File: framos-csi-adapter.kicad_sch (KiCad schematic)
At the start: 68 parts, among them J1 DF40HC(4.0)-60DS-0.4V(51)

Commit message: Bump revision to 1.1.0
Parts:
- C1, C10, C12, C15, C16, C2, C4, C8: value (none) -> C_100n_0402; footprint (none) -> framos-csi-adapter-footprints:0402-cap
- C13, C14, C3, C5, C6, C7: value (none) -> C_22u_0603; footprint (none) -> framos-csi-adapter-footprints:0603-cap
- D1: value (none) -> KP-1608CGCK; footprint (none) -> framos-csi-adapter-footprints:LED_0603
- J2: value (none) -> MSAK24025P30; footprint (none) -> framos-csi-adapter-footprints:MSAK24025P30
- L1, L2: value (none) -> 74479887222C; footprint (none) -> framos-csi-adapter-footprints:L_1008_2520Metric
- MP1, MP2, MP3, MP4: value (none) -> PCB_Mount_Hole_2.2_4.5; footprint (none) -> framos-csi-adapter-footprints:mounting-hole-2.2mm
- N1: value (none) -> oshw_logo; footprint (none) -> framos-csi-adapter-footprints:oshw-logo
- N2: value (none) -> antmicro_logo; footprint (none) -> framos-csi-adapter-footprints:antmicro-logo_scaled_12mm
- R1, R3, R5: value (none) -> R_100k_0402; footprint (none) -> framos-csi-adapter-footprints:0402-res
- R10, R13, R16, R17, R9: value (none) -> R_0R_0402; footprint (none) -> framos-csi-adapter-footprints:0402-res
- R11, R12: value (none) -> R_2k2_0402; footprint (none) -> framos-csi-adapter-footprints:0402-res
- R14: value (none) -> R_37k4_0402; footprint (none) -> framos-csi-adapter-footprints:0402-res
- R15, R19, R4, R6: value (none) -> R_10k_0402; footprint (none) -> framos-csi-adapter-footprints:0402-res
- R18: value (none) -> R_12k4_0402; footprint (none) -> framos-csi-adapter-footprints:0402-res
- R2: value (none) -> R_330R_0402; footprint (none) -> framos-csi-adapter-footprints:0402-res
- R7, R8: value (none) -> R_12k_0402; footprint (none) -> framos-csi-adapter-footprints:0402-res
- TP1, TP10, TP11, TP12, TP13, TP14, TP15, TP16, TP17, TP19, TP2, TP20, TP21, TP3, TP4, TP5, TP6, TP7, TP8, TP9: value (none) -> TP_SMD_0_75MM; footprint (none) -> framos-csi-adapter-footprints:Testpoint_smd_0_75mm
- TP18: value (none) -> TP_SMD1MM; footprint (none) -> framos-csi-adapter-footprints:Testpoint_smd_1mm
- U1: value (none) -> NTS0102GT; footprint (none) -> antmicro-footprints:PSON50P100X195X50-8N
- U2, U3: value (none) -> AP62301Z6-7; footprint (none) -> framos-csi-adapter-footprints:SOT-563
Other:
- title: (none) -> FRAMOS CSI adapter

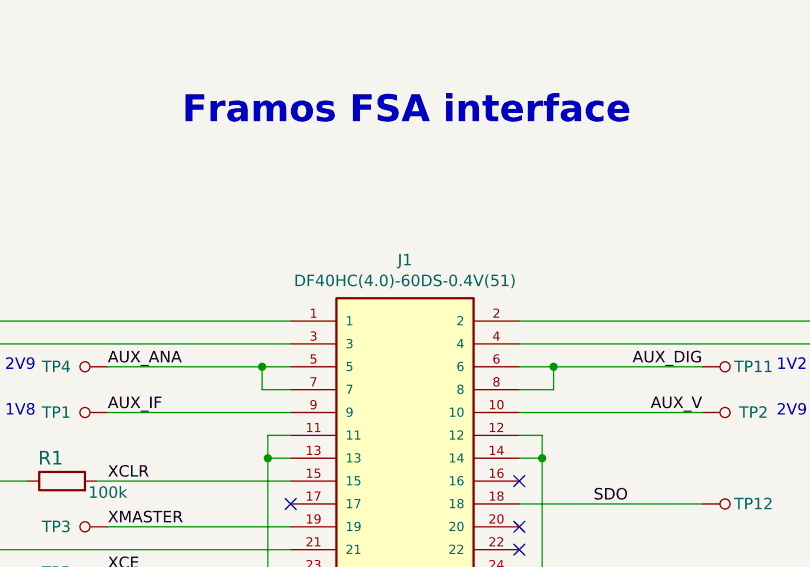
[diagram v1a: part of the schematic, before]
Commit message: Revert PN to DF40C-60DS-0.4V(51)
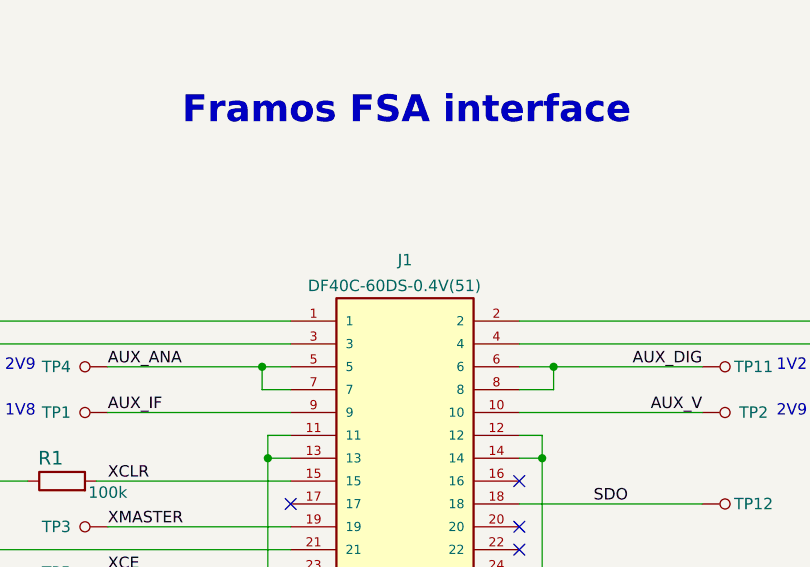
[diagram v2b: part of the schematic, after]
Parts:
- J1: value DF40HC(4.0)-60DS-0.4V(51) -> DF40C-60DS-0.4V(51); symbol antmicroRectangularConnectorsHeadersMalePins:DF40HC(4.0)-60DS-0.4V(51) -> antmicroRectangularConnectorsHeadersMalePins:DF40C-60DS-0.4V(51); MPN DF40HC(4.0)-60DS-0.4V(51) -> DF40C-60DS-0.4V(51)
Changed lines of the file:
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@@
     )
   )
-  (symbol (lib_id "antmicroRectangularConnectorsHeadersMalePins:DF40HC(4.0)-60DS-0.4V(51)") (at 106.045 113.665 0) (unit 1)
+  (symbol (lib_id "antmicroRectangularConnectorsHeadersMalePins:DF40C-60DS-0.4V(51)") (at 106.045 113.665 0) (unit 1)
     (in_bom yes) (on_board yes)
     (property "Reference" "J1" (id 0) (at 106.045 45.9232 0))
-    (property "Value" "DF40HC(4.0)-60DS-0.4V(51)" (id 1) (at 106.045 48.2346 0))
+    (property "Value" "DF40C-60DS-0.4V(51)" (id 1) (at 95.25 49.53 0)
+      (effects (font (size 1.27 1.27)) (justify left bottom))
+    )
     (property "Footprint" "antmicro-footprints:DF40C-60DS-0.4V51" (id 2) (at 106.045 113.665 0)
       (effects (font (size 1.27 1.27)) (justify left bottom) hide)
@@
       (effects (font (size 1.27 1.27)) (justify left bottom) hide)
     )
-    (property "MPN" "DF40HC(4.0)-60DS-0.4V(51)" (id 4) (at 106.045 113.665 0)
+    (property "MPN" "DF40C-60DS-0.4V(51)" (id 4) (at 106.045 113.665 0)
       (effects (font (size 1.27 1.27)) hide)
     )
@@
     )
     (path "/00000000-0000-0000-0000-0000617cc223"
-      (reference "J1") (unit 1) (value "DF40HC(4.0)-60DS-0.4V(51)") (footprint "antmicro-footprints:DF40C-60DS-0.4V51")
+      (reference "J1") (unit 1) (value "DF40C-60DS-0.4V(51)") (footprint "antmicro-footprints:DF40C-60DS-0.4V51")
     )
     (path "/00000000-0000-0000-0000-0000616dc144"

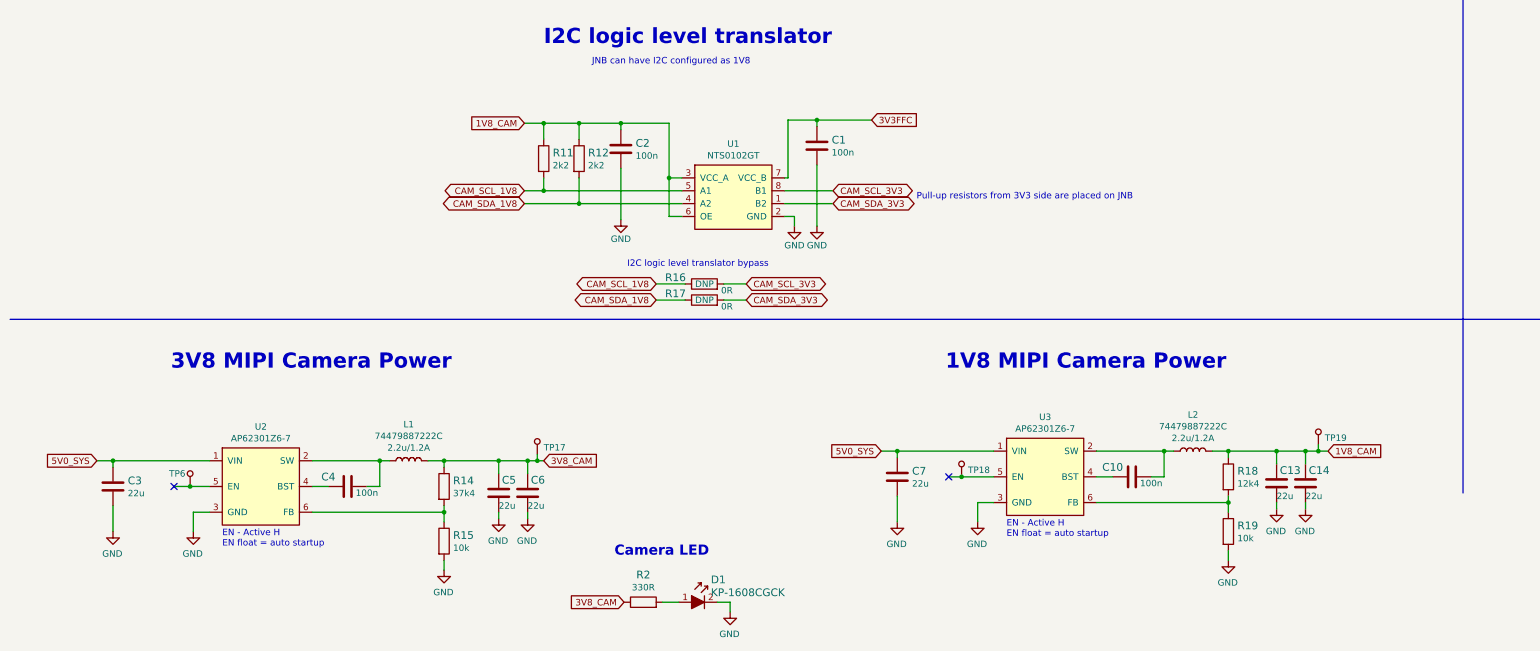
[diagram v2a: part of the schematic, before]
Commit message: Migrate to KiCad 6. Add LICENSE and README. Correct OSHW logo footprint
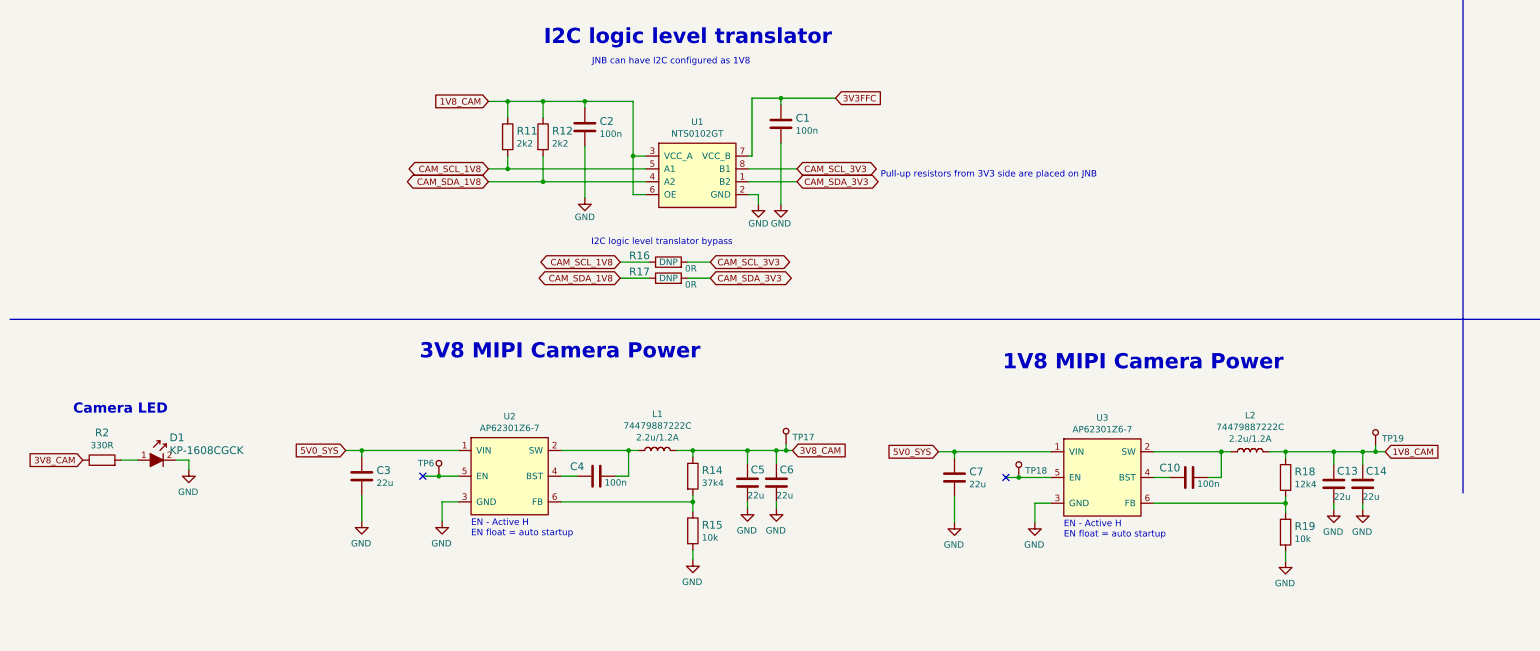
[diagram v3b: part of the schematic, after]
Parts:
- J1: footprint antmicro-footprints:DF40C-60DS-0.4V51 -> framos-csi-adapter-footprints:DF40C-60DS-0.4V51; symbol antmicroRectangularConnectorsHeadersMalePins:DF40C-60DS-0.4V(51) -> framos-csi-adapter:DF40C-60DS-0.4V(51)
- N1: footprint framos-csi-adapter-footprints:oshw-logo -> framos-csi-adapter-footprints:OSHW-Logo2_7.3x6mm_Copper
- U1: footprint antmicro-footprints:PSON50P100X195X50-8N -> framos-csi-adapter-footprints:PSON50P100X195X50-8N
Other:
- moved on the sheet: C1, C10, C13, C14, C2, C3, C4, C5, C6, C7, D1, L1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

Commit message: Cleanup
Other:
- note added: "FRAMOS CSI interposer connector"
- note added: "FRAMOS FSA interface"
- note removed: "Framos CSI interposer connector"
- note removed: "Framos FSA interface"

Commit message: Introduce component standardization
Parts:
- C1, C12, C15, C16, C2, C8: footprint framos-csi-adapter-footprints:0402-cap -> framos-csi-adapter-footprints:C_0402_1005Metric; Author (none) -> Antmicro; Dielectric (none) -> X5R; License (none) -> Apache-2.0; MPN 0402X104K6R3CT -> GRM155R61H104KE14D; Manufacturer Walsin -> Murata; Voltage (none) -> 50V
- C10, C4: footprint framos-csi-adapter-footprints:0402-cap -> framos-csi-adapter-footprints:C_0402_1005Metric; Author (none) -> Antmicro; Dielectric (none) -> X5R; License (none) -> Apache-2.0; Voltage (none) -> 50V
- C13, C14, C3, C5, C6, C7: footprint framos-csi-adapter-footprints:0603-cap -> framos-csi-adapter-footprints:C_0603_1608Metric; Author (none) -> Antmicro; License (none) -> Apache-2.0; Manufacturer MURATA -> Murata
- D1: value KP-1608CGCK -> LED_G_0603_KP-1608CGCK; footprint framos-csi-adapter-footprints:LED_0603 -> framos-csi-adapter-footprints:LED_0603_1608Metric_G; symbol framos-csi-adapter:KP-1608CGCK -> framos-csi-adapter:LED_G_0603_KP-1608CGCK; Author (none) -> Antmicro; License (none) -> Apache-2.0; Manufacturer KINGBRIGHT -> Kingbright
- J1: value DF40C-60DS-0.4V(51) -> Conn_Hirose_DF40C-60DS-0.4V51; footprint framos-csi-adapter-footprints:DF40C-60DS-0.4V51 -> framos-csi-adapter-footprints:Conn_Hirose_DF40C-60DS-0.4V51; symbol framos-csi-adapter:DF40C-60DS-0.4V(51) -> framos-csi-adapter:Conn_Hirose_DF40C-60DS-0.4V51; Author (none) -> Antmicro; License (none) -> Apache-2.0; Manufacturer HRS -> Hirose
- J2: value MSAK24025P30 -> Conn_STM_MSAK24025P30; footprint framos-csi-adapter-footprints:MSAK24025P30 -> framos-csi-adapter-footprints:Conn_STM_MSAK24025P30; symbol framos-csi-adapter:MSAK24025P30 -> framos-csi-adapter:Conn_STM_MSAK24025P30; Author (none) -> Antmicro; License (none) -> Apache-2.0; Manufacturer STM -> STMicroelectronics
- L1, L2: Author (none) -> Antmicro; License (none) -> Apache-2.0; Manufacturer Wurth Elektronik -> Würth Elektronik; MaxCur 1.2A -> (none); Value2 2.2u/1.2A -> (none)
- MP1, MP2, MP3, MP4, N2, U2, U3: Author (none) -> Antmicro; License (none) -> Apache-2.0
- N1: footprint framos-csi-adapter-footprints:OSHW-Logo2_7.3x6mm_Copper -> framos-csi-adapter-footprints:OSHW-Logo2_7.3x6mm_Copper_Mask; Author (none) -> Antmicro; License (none) -> Apache-2.0
- R1, R3, R5: footprint framos-csi-adapter-footprints:0402-res -> framos-csi-adapter-footprints:R_0402_1005Metric; Author (none) -> Antmicro; License (none) -> Apache-2.0; MPN CRCW0402100KFKEDHP -> CR0402-FX-1003GLF; Manufacturer VISHAY -> Bourns; Tolerance (none) -> 1%
- R10, R13, R16, R17, R9: footprint framos-csi-adapter-footprints:0402-res -> framos-csi-adapter-footprints:R_0402_1005Metric; Author (none) -> Antmicro; Current (none) -> 1A; License (none) -> Apache-2.0; Manufacturer PANASONIC -> Panasonic
- R11, R12: footprint framos-csi-adapter-footprints:0402-res -> framos-csi-adapter-footprints:R_0402_1005Metric; Author (none) -> Antmicro; License (none) -> Apache-2.0; MPN RC0402FR-072K2L -> CR0402-FX-2201GLF; Manufacturer YAGEO -> Bourns; Tolerance (none) -> 1%
- R14: footprint framos-csi-adapter-footprints:0402-res -> framos-csi-adapter-footprints:R_0402_1005Metric; Author (none) -> Antmicro; License (none) -> Apache-2.0; MPN RC0402FR-0737K4L -> CR0402-FX-3742GLF; Manufacturer Yageo -> Bourns; Tolerance (none) -> 1%
- R15, R19, R4, R6: footprint framos-csi-adapter-footprints:0402-res -> framos-csi-adapter-footprints:R_0402_1005Metric; Author (none) -> Antmicro; License (none) -> Apache-2.0; MPN CRCW040210K0FKEDHP -> CR0402-FX-1002GLF; Manufacturer VISHAY -> Bourns; Tolerance (none) -> 1%
- R18: footprint framos-csi-adapter-footprints:0402-res -> framos-csi-adapter-footprints:R_0402_1005Metric; Author (none) -> Antmicro; License (none) -> Apache-2.0; MPN ERJ2RKF1242X -> CR0402-FX-1242GLF; Manufacturer PANASONIC_ELECTRONIC_COMPONENTS -> Bourns; Tolerance (none) -> 1%
- R2: footprint framos-csi-adapter-footprints:0402-res -> framos-csi-adapter-footprints:R_0402_1005Metric; Author (none) -> Antmicro; License (none) -> Apache-2.0; MPN MCMR04X3300FTL -> CR0402-FX-3300GLF; Manufacturer MULTICOMP -> Bourns; Tolerance (none) -> 1%
- R7, R8: footprint framos-csi-adapter-footprints:0402-res -> framos-csi-adapter-footprints:R_0402_1005Metric; Author (none) -> Antmicro; License (none) -> Apache-2.0; MPN CRCW040212K0FKEDHP -> CR0402-FX-1202GLF; Manufacturer VISHAY -> Bourns; Tolerance (none) -> 1%
- TP1, TP10, TP11, TP12, TP13, TP14, TP15, TP16, TP17, TP19, TP2, TP20, TP21, TP3, TP4, TP5, TP6, TP7, TP8, TP9: value TP_SMD_0_75MM -> TP_0.75mm_SMD; footprint framos-csi-adapter-footprints:Testpoint_smd_0_75mm -> framos-csi-adapter-footprints:TP_SMD_0.75mm; symbol framos-csi-adapter:TP_SMD_0_75MM -> framos-csi-adapter:TP_0.75mm_SMD; Author (none) -> Antmicro; License (none) -> Apache-2.0
- TP18: value TP_SMD1MM -> TP_1mm_SMD; symbol framos-csi-adapter:TP_SMD1MM -> framos-csi-adapter:TP_1mm_SMD; Author (none) -> Antmicro; License (none) -> Apache-2.0
- U1: value NTS0102GT -> NTS0102_XSON; footprint framos-csi-adapter-footprints:PSON50P100X195X50-8N -> framos-csi-adapter-footprints:XSON-8_1x1.95mm_P0.5mm; symbol framos-csi-adapter:NTS0102GT -> framos-csi-adapter:NTS0102_XSON; Author (none) -> Antmicro; License (none) -> Apache-2.0; Manufacturer NXP Semiconductors -> NXP
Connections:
- net 1V8_CAM: now also R3.1; no longer R3.2
- net PW_EN_1: now also R3.2; no longer R3.1
- net at L1.1, U2.2 (SW): now also C4.2; no longer C4.1
- net at U2.4 (BST): now also C4.1; no longer C4.2
- net at L2.1, U3.2 (SW): now also C10.2; no longer C10.1
- net at U3.4 (BST): now also C10.1; no longer C10.2
- no-connect marks 13 -> 11
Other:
- moved on the sheet: C1, C10, C12, C13, C14, C15, C16, C2, C3, C4, C5, C6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
